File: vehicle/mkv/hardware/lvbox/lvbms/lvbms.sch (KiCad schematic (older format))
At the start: 147 parts, among them J1 CONN_02X03, J2 NanoFit_RA_SMT_04, J3 NanoFit_RA_SMT_02, J4 NanoFit_RA_SMT_02, J5 NanoFit_RA_SMT_02, J6 NanoFit_RA_SMT_02, J7 NanoFit_RA_SMT_02, J8 NanoFit_RA_SMT_06_A, J9 NanoFit_RA_SMT_02, Q1 NSS1C201MZ4, Q10 SSM3K333R, Q2 SQM110P06, Q3 SSM3K333R, Q4 SSM3K333R, Q5 SQM110P06, Q6 BSS138, Q7 SQM110P06, Q8 SQM110P06, Q9 SSM3K333R, U1 MCP2561-E_SN, U10 ACHS-7124, U11 redcube-7461057, U2 ATMEGA16M1, U3 LTC6810HG-2, U4 LT3066IMSE-5, U5 LT1017IS8, U9 redcube-7461057, Y1 Crystal_SMD

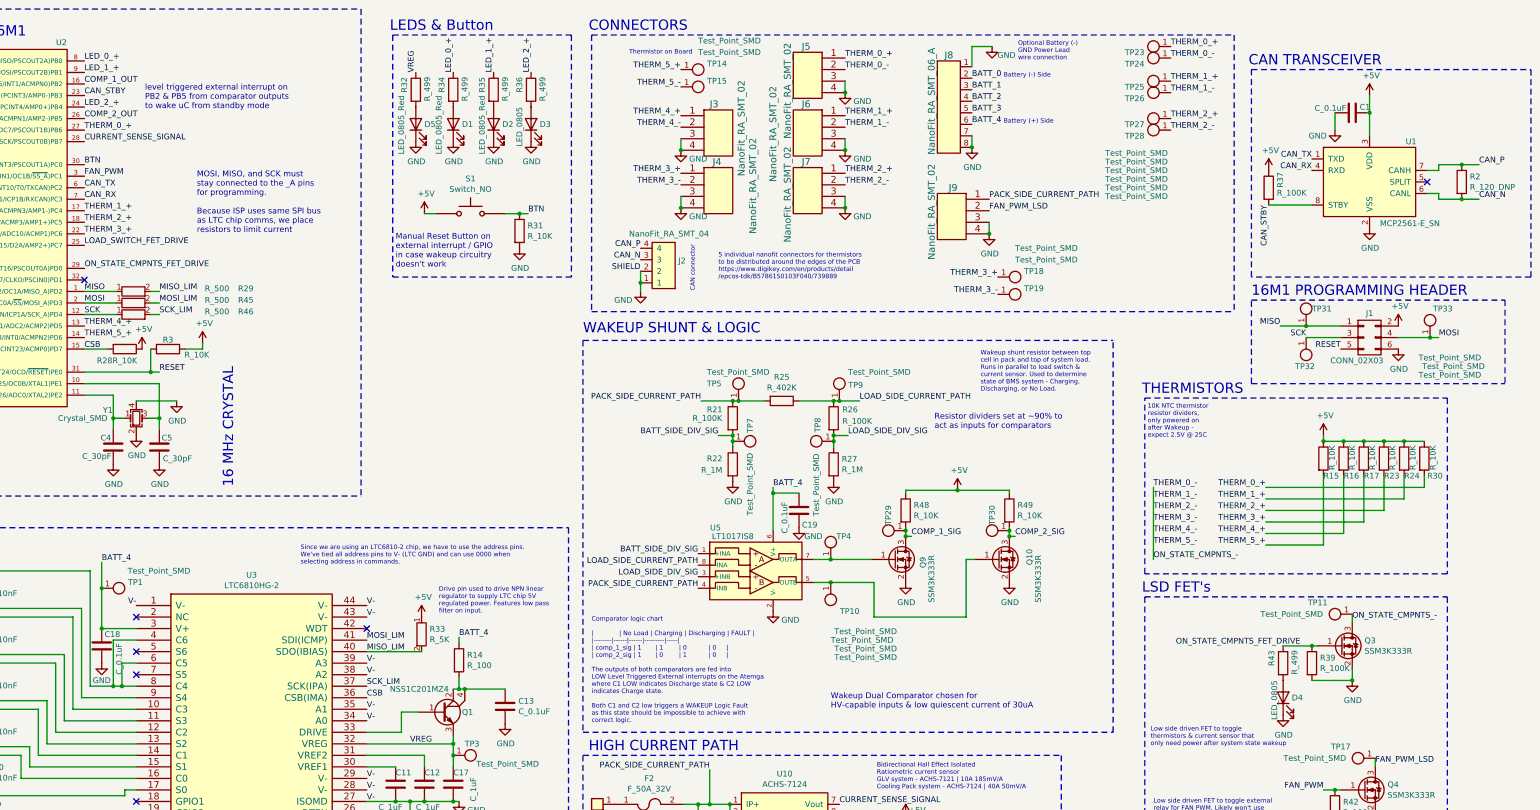
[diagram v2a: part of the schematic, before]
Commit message: schem changes, + code updates for default SPI peripheral + testing
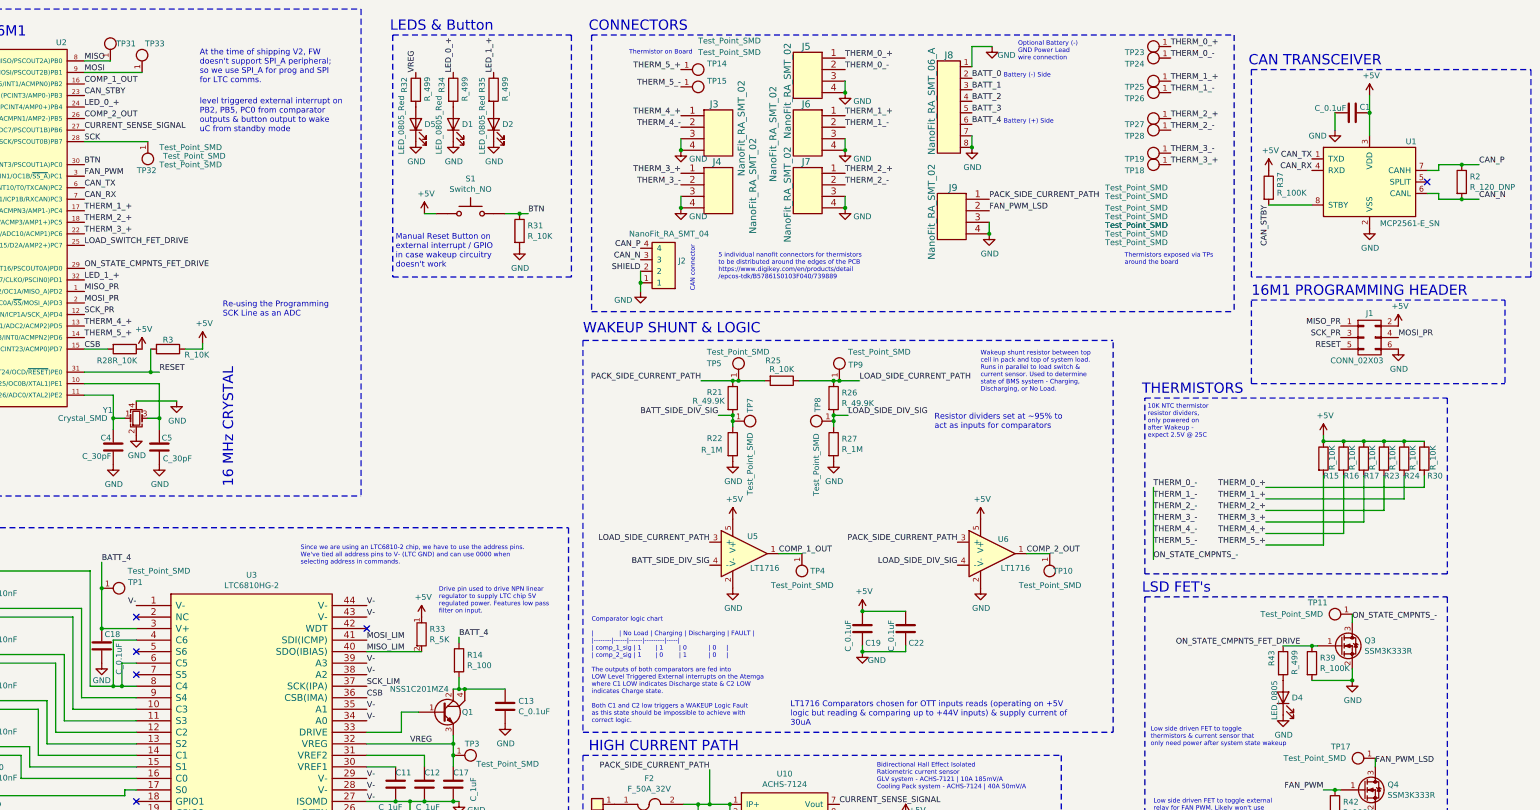
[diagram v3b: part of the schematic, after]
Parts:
- removed D3: LED_0805, footprints:LED_0805_OEM, symbol formula:LED_0805
- removed Q10, Q9: SSM3K333R, footprints:SOT-23F, symbol formula:SSM3K333R
- removed R21, R26: R_100K, footprints:R_0805_OEM, symbol formula:R_100K
- removed R25: R_402K, footprints:R_0805_OEM, symbol formula:R_402K
- removed R29, R45, R46: R_500, footprints:R_0805_OEM, symbol formula:R_500
- removed R36: R_499, footprints:R_0805_OEM, symbol formula:R_499
- removed R48, R49: R_10K, footprints:R_0805_OEM, symbol formula:R_10K
- removed TP29, TP30: Test_Point_SMD, TestPoint:TestPoint_Pad_D1.5mm, symbol formula:Test_Point_SMD
- removed U5: LT1017IS8, footprints:SO-8_S, symbol formula:LT1017IS8
- added C22: C_0.1uF, footprints:C_0805_OEM, symbol formula:C_0.1uF
- added R21, R26: R_49.9K, footprints:R_0805_OEM, symbol formula:R_49.9K
- added R25: R_10K, footprints:R_0805_OEM, symbol formula:R_10K
- added U5, U6: LT1716, Package_TO_SOT_SMD:SOT-23-5, symbol formula:LT1716
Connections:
- net LED_2_+ is gone; now on net LED_0_+: U2.24 ((PCINT4/AMP0+)PB4)
- net +5V: now also C19.1, C22.1, U5.5 (V+), U6.5 (V+)
- net BATT_4: no longer C19.1
- net BATT_SIDE_DIV_SIG: now also R21.2, U5.4 (-)
- net COMP_1_OUT: now also TP4.1, U5.1
- net COMP_2_OUT: now also TP10.1, U6.1
- net CURRENT_SENSE_SIGNAL: now also U2.27 ((PCINT6/ADC7/PSCOUT1B)PB6); no longer U2.28 ((PCINT7/ADC4/SCK/PSCOUT0B)PB7)
- net GND: now also C22.2, U5.2 (V-), U6.2 (V-)
- net LED_0_+: no longer U2.8 ((PCINT0/MISO/PSCOUT2A)PB0)
- net LED_1_+: now also U2.32 ((PCINT17/CLKO/PSCIN0)PD1); no longer U2.9 ((PCINT1/MOSI/PSCOUT2B)PB1)
- net LOAD_SIDE_CURRENT_PATH: now also R25.1, R26.1, U5.3 (+)
- net LOAD_SIDE_DIV_SIG: now also R26.2, U6.4 (-)
- net MISO: now also U2.8 ((PCINT0/MISO/PSCOUT2A)PB0); no longer J1.1 (P1), U2.1 ((PCINT18/PSCIN2/OC1A/MISO_A)PD2)
- net MOSI: now also U2.9 ((PCINT1/MOSI/PSCOUT2B)PB1); no longer J1.4 (P4), U2.2 ((PCINT19/TXD/TXLIN/OC0A/~SS~/MOSI_A)PD3)
- net PACK_SIDE_CURRENT_PATH: now also R21.1, R25.2, U6.3 (+)
- net SCK: now also U2.28 ((PCINT7/ADC4/SCK/PSCOUT0B)PB7); no longer J1.3 (P3), U2.12 ((PCINT20/ADC1/RXD/RXLIN/ICP1A/SCK_A)PD4)
- net THERM_0_+: no longer U2.27 ((PCINT6/ADC7/PSCOUT1B)PB6)
- new net MISO_PR: J1.1 (P1), U2.1 ((PCINT18/PSCIN2/OC1A/MISO_A)PD2)
- new net MOSI_PR: J1.4 (P4), U2.2 ((PCINT19/TXD/TXLIN/OC0A/~SS~/MOSI_A)PD3)
- new net SCK_PR: J1.3 (P3), U2.12 ((PCINT20/ADC1/RXD/RXLIN/ICP1A/SCK_A)PD4)
- no-connect marks 13 -> 12
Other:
- note added: "At the time of shipping V2, FW \ndoesn't support SPI_A peripheral; \nso we use SPI_A for prog and SPI\nfor LTC comms."
- note added: "LT1716 Comparators chosen for OTT inputs reads (operating on +5V\nlogic but reading & comparing up to +44V inputs) & supply current of\n30uA"
- note added: "Re-using the Programming \nSCK Line as an ADC"
- note added: "Resistor dividers set at ~~95% to \nact as inputs for comparators"
- note added: "Thermistors exposed via TPs\naround the board"
- note added: "level triggered external interrupt on \nPB2, PB5, PC0 from comparator \noutputs & button output to wake \nuC from standby mode\n"
- note removed: "MOSI, MISO, and SCK must\nstay connected to the _A pins\nfor programming.\n\nBecause ISP uses same SPI bus \nas LTC chip comms, we place \nresistors to limit current"
- note removed: "Resistor dividers set at ~~90% to \nact as inputs for comparators"
- note removed: "Wakeup Dual Comparator chosen for\nHV-capable inputs & low quiescent current of 30uA"
- note removed: "level triggered external interrupt on \nPB2 & PB5 from comparator outputs\nto wake uC from standby mode\n"
- moved on the sheet: C19, R22, R27, TP18, TP19, TP31, TP32, TP33, TP5, TP7, TP8, TP9

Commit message: completed rev2 first pass, ship soon hopefully! <3
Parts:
- removed J5: NanoFit_RA_SMT_02, footprints:NanoFit_RA_SMT_02, symbol formula:NanoFit_RA_SMT_02
- removed R44, R47: R_0, footprints:R_0603_1608Metric, symbol formula:R_0
- added R29: R_0_2512, footprints:R_2512_OEM, symbol formula:R_0_2512
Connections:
- net BATT_0 is gone; now on net GND: J8.2, R13.2, R8.2
- net MISO_LIM is gone; now on net MISO: R33.2, U3.40 (SDO(IBIAS))
- net MOSI_LIM is gone; now on net MOSI: U3.41 (SDI(ICMP))
- net SCK_LIM is gone; now on net SCK: U3.37 (SCK(IPA))
- net +5V: now also R31.1; no longer S1.1, S1.2
- net BATT_4: now also R29.2
- net BTN: now also R31.2, S1.1, S1.2; no longer R31.1, S1.3, S1.4
- net GND: now also S1.3, S1.4; no longer R31.2
- net PACK_SIDE_CURRENT_PATH: now also R29.1
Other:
- note added: "Jumper for testing only! \nDNP before use!"
- note added: "Manual Reset Button on \nexternal interrupt / GPIO \nin case wakeup circuitry \ndoesn't work, default HIGH"
- note removed: "Manual Reset Button on \nexternal interrupt / GPIO \nin case wakeup circuitry \ndoesn't work"
- moved on the sheet: R31, TP31
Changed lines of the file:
@@
 	6600 7025 6600 7125
 Text Label 6100 6025 0    50   ~ 0
-MOSI_LIM
+MOSI
 Text Label 6100 6425 0    50   ~ 0
-SCK_LIM
+SCK
 Text Label 6100 6525 0    50   ~ 0
 CSB
@@
 	13925 2250 14300 2250
 Text Label 6100 6125 0    50   ~ 0
-MISO_LIM
+MISO
 Wire Wire Line
 	2700 5825 2800 5825
@@
 Text Label 3650 3400 0    50   ~ 0
 THERM_5_+
-Text Label 10250 975  0    50   ~ 0
-THERM_0_+
-Text Label 10250 1075 0    50   ~ 0
-THERM_0_-
 Text Label 10250 1475 0    50   ~ 0
 THERM_1_+
@@
 L power:GND #PWR?
 U 1 1 61C1271C
-P 1875 7275
-F 0 "#PWR?" H 1875 7025 50  0001 C CNN
-F 1 "GND" H 1880 7102 50  0000 C CNN
-F 2 "" H 1875 7275 50  0001 C CNN
-F 3 "" H 1875 7275 50  0001 C CNN
-	1    1875 7275
+P 1500 7400
+F 0 "#PWR?" H 1500 7150 50  0001 C CNN
+F 1 "GND" H 1625 7350 50  0000 C CNN
+F 2 "" H 1500 7400 50  0001 C CNN
+F 3 "" H 1500 7400 50  0001 C CNN
+	1    1500 7400
 	1    0    0    -1
 $EndComp
@@
 	1    0    0    -1
 $EndComp
-Text Notes 8000 9325 0    47   ~ 0
+Text Notes 8000 9625 0    47   ~ 0
 The high current path on this \nPCB will see 20A continuous, \n30A peak for 1 hour with the \ncooling pack, and 5A continuous \nwith the GLV pack. Our high \ncurrent path features a current \nsensor, bidirectional load switch, \nand fuse.  \n\nThe fuse and current sensor are \ndifferent between GLV system \nand cooling pack system. \n\nThe bidirectional load switch was \ntested with the LV BMS Tester \nBoard. As a switch, it functionally \nworks, but thermals still need to \nbe tested on this PCB.
 Wire Notes Line
@@
 Text Notes 6900 9450 0    39   ~ 0
 Linreg will dissipate 2.35W \nnominally continuously w/\nsystem in ON state. \nWith 400mm Cu, an Rth J-A \nof 37C/W, Junction temp \n=86.95C
-Wire Wire Line
-	2150 7325 2150 7375
-Wire Wire Line
-	2150 7375 4000 7375
-Wire Wire Line
-	4000 7375 4000 7325
-Wire Wire Line
-	4000 7325 4100 7325
 $Comp
 L power:GND #PWR?
@@
 U 1 1 61FA96DC
 P 2150 7175
-F 0 "R8" V 2200 7350 50  0000 R CNN
-F 1 "R_15_1W_.5%" V 2125 7750 50  0000 R CNN
+F 0 "R8" V 2125 7350 50  0000 R CNN
+F 1 "R_15_1W_.5%" V 2200 7750 50  0000 R CNN
 F 2 "footprints:Fuse_1206" H 2150 7425 50  0001 C CNN
 F 3 "https://www.susumu.co.jp/common/pdf/n_catalog_partition24_en.pdf" H 2150 7275 50  0001 C CNN
@@
 $EndComp
 $Comp
-L formula:NanoFit_RA_SMT_02 J5
-U 1 1 61F6DB51
-P 10250 975
-F 0 "J5" H 10550 1075 60  0000 L CNN
-F 1 "NanoFit_RA_SMT_02" V 10750 275 60  0000 L CNN
-F 2 "footprints:NanoFit_RA_SMT_02" H 10650 475 60  0001 C CNN
-F 3 "http://www.literature.molex.com/SQLImages/kelmscott/Molex/PDF_Images/987651-1223.PDF" H 10250 975 60  0001 C CNN
-F 4 "1054301102" H 10450 275 50  0001 C CNN "MPN"
-F 5 "https://www.digikey.com/en/products/detail/molex/1054301102/9959376" H 10300 375 50  0001 C CNN "Purchasing Link"
-	1    10250 975
-	-1   0    0    -1
-$EndComp
-$Comp
 L formula:NanoFit_RA_SMT_02 J6
 U 1 1 61FE69F9
@@
 	10250 1675 10250 1775
 Wire Wire Line
-	10250 1175 10250 1275
-Wire Wire Line
 	8825 1675 8825 1775
 Wire Wire Line
@@
 $Comp
 L power:GND #PWR?
-U 1 1 620F6E21
-P 10250 1275
-F 0 "#PWR?" H 10250 1025 50  0001 C CNN
-F 1 "GND" H 10400 1200 50  0000 C CNN
-F 2 "" H 10250 1275 50  0001 C CNN
-F 3 "" H 10250 1275 50  0001 C CNN
-	1    10250 1275
-	1    0    0    -1
-$EndComp
-$Comp
-L power:GND #PWR?
 U 1 1 6210B498
 P 10250 1775
@@
 $EndComp
 Connection ~ 10250 1775
-Connection ~ 10250 1275
 Connection ~ 8825 1775
 Connection ~ 8825 2275
@@
 Wire Notes Line
 	8050 775  8050 3175
-$Comp
-L formula:R_0 R44
-U 1 1 6223F8F7
-P 1650 7275
-F 0 "R44" V 1725 7225 50  0000 C CNN
-F 1 "R_0" V 1800 7250 50  0000 C CNN
-F 2 "footprints:R_0603_1608Metric" H 1580 7275 50  0001 C CNN
-F 3 "http://industrial.panasonic.com/www-cgi/jvcr13pz.cgi?E+PZ+3+AOA0001+ERJ3GEY0R00V+7+WW" H 1730 7275 50  0001 C CNN
-F 4 "DK" H 1650 7275 60  0001 C CNN "MFN"
-F 5 "P0.0GCT-ND" H 1650 7275 60  0001 C CNN "MPN"
-F 6 "https://www.digikey.com/product-detail/en/panasonic-electronic-components/ERJ-3GEY0R00V/P0.0GCT-ND/134711" H 2130 7675 60  0001 C CNN "PurchasingLink"
-	1    1650 7275
-	0    1    1    0
-$EndComp
-Wire Wire Line
-	1500 7025 1500 7275
-Wire Wire Line
-	1800 7275 1875 7275
 Text Notes 11750 1000 0    39   ~ 0
 Optional Battery (-)\nGND Power Lead \nwire connection
@@
 Wire Wire Line
 	8975 7450 9075 7450
-$Comp
-L formula:R_0 R47
-U 1 1 62672ADF
-P 8975 7700
-F 0 "R47" H 9045 7746 50  0000 L CNN
-F 1 "R_0" H 9045 7655 50  0000 L CNN
-F 2 "footprints:R_0603_1608Metric" H 8905 7700 50  0001 C CNN
-F 3 "http://industrial.panasonic.com/www-cgi/jvcr13pz.cgi?E+PZ+3+AOA0001+ERJ3GEY0R00V+7+WW" H 9055 7700 50  0001 C CNN
-F 4 "DK" H 8975 7700 60  0001 C CNN "MFN"
-F 5 "P0.0GCT-ND" H 8975 7700 60  0001 C CNN "MPN"
-F 6 "https://www.digikey.com/product-detail/en/panasonic-electronic-components/ERJ-3GEY0R00V/P0.0GCT-ND/134711" H 9455 8100 60  0001 C CNN "PurchasingLink"
-	1    8975 7700
-	1    0    0    -1
-$EndComp
 Text Label 8825 7850 2    50   ~ 0
 BATT_4
@@
 L formula:Test_Point_SMD TP31
 U 1 1 62705BA6
-P 3875 950
-F 0 "TP31" H 3925 1050 50  0000 L CNN
-F 1 "Test_Point_SMD" H 4300 150 50  0000 L CNN
-F 2 "TestPoint:TestPoint_Pad_D1.5mm" H 3875 800 50  0001 C CNN
-F 3 "" H 3875 950 50  0001 C CNN
-	1    3875 950
+P 3925 950
+F 0 "TP31" H 3975 1050 50  0000 L CNN
+F 1 "Test_Point_SMD" H 4350 150 50  0000 L CNN
+F 2 "TestPoint:TestPoint_Pad_D1.5mm" H 3925 800 50  0001 C CNN
+F 3 "" H 3925 950 50  0001 C CNN
+	1    3925 950
 	1    0    0    -1
 $EndComp
@@
 $EndComp
 $Comp
-L power:+5V #PWR?
-U 1 1 62717530
-P 6600 2325
-F 0 "#PWR?" H 6600 2175 50  0001 C CNN
-F 1 "+5V" H 6615 2498 50  0000 C CNN
-F 2 "" H 6600 2325 50  0001 C CNN
-F 3 "" H 6600 2325 50  0001 C CNN
-	1    6600 2325
-	1    0    0    -1
-$EndComp
-$Comp
 L formula:R_10K R31
 U 1 1 6271884C
-P 7425 2475
-F 0 "R31" H 7495 2521 50  0000 L CNN
-F 1 "R_10K" H 7495 2430 50  0000 L CNN
-F 2 "footprints:R_0805_OEM" H 7355 2475 50  0001 C CNN
-F 3 "http://www.bourns.com/data/global/pdfs/CRS.pdf" H 7505 2475 50  0001 C CNN
-F 4 "DK" H 7425 2475 60  0001 C CNN "MFN"
-F 5 "CRS0805-FX-1002ELFCT-ND" H 7425 2475 60  0001 C CNN "MPN"
-F 6 "https://www.digikey.com/products/en?keywords=CRS0805-FX-1002ELFCT-ND" H 7905 2875 60  0001 C CNN "PurchasingLink"
-	1    7425 2475
+P 6575 2175
+F 0 "R31" H 6645 2221 50  0000 L CNN
+F 1 "R_10K" H 6645 2130 50  0000 L CNN
+F 2 "footprints:R_0805_OEM" H 6505 2175 50  0001 C CNN
+F 3 "http://www.bourns.com/data/global/pdfs/CRS.pdf" H 6655 2175 50  0001 C CNN
+F 4 "DK" H 6575 2175 60  0001 C CNN "MFN"
+F 5 "CRS0805-FX-1002ELFCT-ND" H 6575 2175 60  0001 C CNN "MPN"
+F 6 "https://www.digikey.com/products/en?keywords=CRS0805-FX-1002ELFCT-ND" H 7055 2575 60  0001 C CNN "PurchasingLink"
+	1    6575 2175
 	1    0    0    -1
 $EndComp
@@
 L power:GND #PWR?
 U 1 1 6271A872
-P 7425 2625
-F 0 "#PWR?" H 7425 2375 50  0001 C CNN
-F 1 "GND" H 7430 2452 50  0000 C CNN
-F 2 "" H 7425 2625 50  0001 C CNN
-F 3 "" H 7425 2625 50  0001 C CNN
-	1    7425 2625
-	1    0    0    -1
-$EndComp
-Wire Wire Line
-	6600 2325 6700 2325
-Wire Wire Line
-	7300 2325 7425 2325
-Wire Wire Line
-	7425 2325 7500 2325
-Connection ~ 7425 2325
-Text Label 7500 2325 0    50   ~ 0
+P 7500 2325
+F 0 "#PWR?" H 7500 2075 50  0001 C CNN
+F 1 "GND" H 7505 2152 50  0000 C CNN
+F 2 "" H 7500 2325 50  0001 C CNN
+F 3 "" H 7500 2325 50  0001 C CNN
+	1    7500 2325
+	1    0    0    -1
+$EndComp
+Text Label 6500 2325 2    50   ~ 0
 BTN
 Wire Notes Line
@@
 	7875 775  7875 2875
 Text Notes 6350 2800 0    50   ~ 0
-Manual Reset Button on \nexternal interrupt / GPIO \nin case wakeup circuitry \ndoesn't work
+Manual Reset Button on \nexternal interrupt / GPIO \nin case wakeup circuitry \ndoesn't work, default HIGH
 Wire Notes Line
 	6050 550  6050 4775
@@
 U 1 1 628CBBA9
 P 12025 5325
-F 0 "TP10" H 11825 5425 50  0000 L CNN
+F 0 "TP10" H 11775 5425 50  0000 L CNN
 F 1 "Test_Point_SMD" H 11750 5550 50  0000 L CNN
 F 2 "TestPoint:TestPoint_Pad_D1.5mm" H 12025 5175 50  0001 C CNN
@@
 MOSI
 Wire Wire Line
-	3650 1000 3875 1000
-Wire Wire Line
 	3650 1100 4150 1100
 Wire Wire Line
@@
 	0    1    1    0
 $EndComp
+Wire Wire Line
+	1500 7400 2700 7400
+Connection ~ 2700 7400
+Wire Wire Line
+	1500 7025 1500 7400
+Connection ~ 1500 7400
+Wire Wire Line
+	2150 7325 4100 7325
+$Comp
+L formula:R_0_2512 R29
+U 1 1 627191D8
+P 8975 7700
+F 0 "R29" H 8800 7750 50  0000 L CNN
+F 1 "R_0_2512" H 8550 7675 50  0000 L CNN
+F 2 "footprints:R_2512_OEM" H 8905 7700 50  0001 C CNN
+F 3 "http://www.te.com/commerce/DocumentDelivery/DDEController?Action=srchrtrv&DocNm=9-1773463-7&DocType=DS&DocLang=English" H 9055 7700 50  0001 C CNN
+F 4 "DK" H 8975 7700 60  0001 C CNN "MFN"
+F 5 "A121322CT-ND" H 8975 7700 60  0001 C CNN "MPN"
+F 6 "https://www.digikey.com/products/en?keywords=A121322CT-ND" H 9455 8100 60  0001 C CNN "PurchasingLink"
+	1    8975 7700
+	1    0    0    -1
+$EndComp
+Text Notes 8175 8050 0    47   ~ 0
+Jumper for testing only! \nDNP before use!
+Wire Wire Line
+	3650 1000 3925 1000
+Wire Wire Line
+	6500 2325 6575 2325
+Wire Wire Line
+	7300 2325 7500 2325
+Connection ~ 6575 2325
+Wire Wire Line
+	6575 2325 6700 2325
+$Comp
+L power:+5V #PWR?
+U 1 1 626E83E7
+P 6575 2025
+F 0 "#PWR?" H 6575 1875 50  0001 C CNN
+F 1 "+5V" H 6700 2100 50  0000 C CNN
+F 2 "" H 6575 2025 50  0001 C CNN
+F 3 "" H 6575 2025 50  0001 C CNN
+	1    6575 2025
+	1    0    0    -1
+$EndComp
 $EndSCHEMATC

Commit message: removed joke
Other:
- note removed: "~I will get shafted on this design review.~ -Adi R."
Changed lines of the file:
@@
 Text Notes 12900 6950 0    39   ~ 0
 Low side driven FET to toggle \nthermistors & current sensor that\nonly need power after system state wakeup
-Text Notes 12300 9425 0    39   ~ 0
-~I will get shafted on this design review.~ -Adi R.
 Wire Wire Line
 	6850 7425 6900 7425
